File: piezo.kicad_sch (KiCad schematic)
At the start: 0 parts

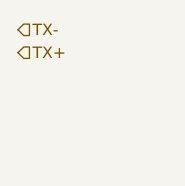
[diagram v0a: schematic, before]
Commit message: Finished schematic, added power section for external power (both power supply and battery), added current sensing for TX microcontroller
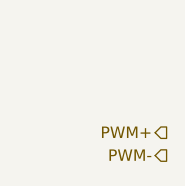
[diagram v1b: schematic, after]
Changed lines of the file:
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@@
 		(company "UVM SEED Team 512 - NWTL")
 	)
-	(hierarchical_label "TX+"
-		(shape input)
-		(at 123.19 86.36 0)
+	(hierarchical_label "PWM+"
+		(shape output)
+		(at 139.7 95.25 180)
 		(effects
 			(font
 				(size 1.27 1.27)
 			)
-			(justify left)
+			(justify right)
 		)
 	)
-	(hierarchical_label "TX-"
-		(shape input)
-		(at 123.19 83.82 0)
+	(hierarchical_label "PWM-"
+		(shape output)
+		(at 139.7 97.79 180)
 		(effects
 			(font
 				(size 1.27 1.27)
 			)
-			(justify left)
+			(justify right)
 		)
 	)
